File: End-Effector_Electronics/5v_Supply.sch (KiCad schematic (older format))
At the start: 0 parts

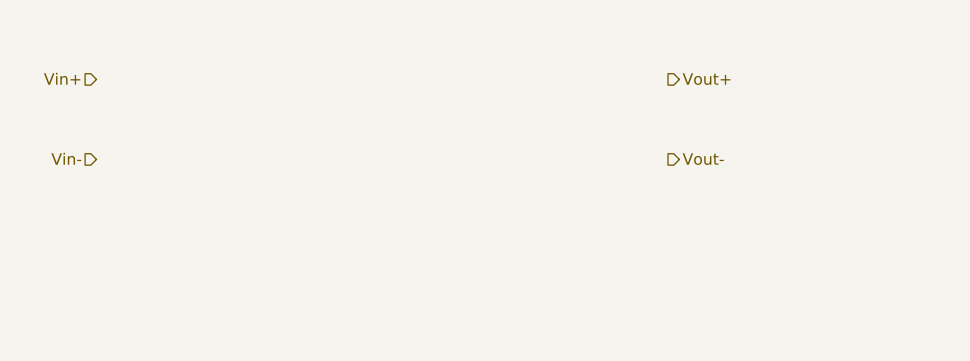
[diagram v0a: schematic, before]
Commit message: 5V supply added
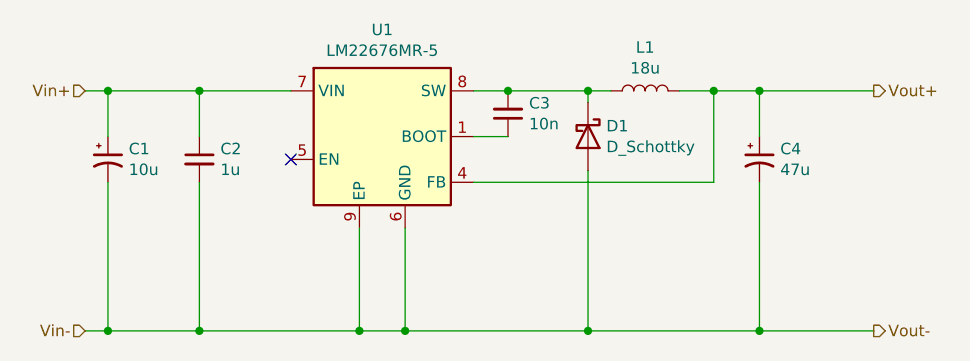
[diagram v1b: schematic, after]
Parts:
- added C1: 10u, symbol Device:CP1_Small
- added C2: 1u, symbol Device:C_Small
- added C3: 10n, symbol Device:C_Small
- added C4: 47u, symbol Device:CP1_Small
- added D1: D_Schottky, symbol Device:D_Schottky
- added L1: 18u, symbol Device:L
- added U1: LM22676MR-5, Package_SO:TI_SO-PowerPAD-8, symbol Regulator_Switching:LM22676MR-5
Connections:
- net Vin+: now also C1.1, C2.1, U1.7 (VIN)
- net Vin-: now also C1.2, C2.2, C4.2, D1.2 (A), U1.6 (GND), U1.9 (EP)
- net Vout+: now also C4.1, L1.2, U1.4 (FB)
- new net: C3.1, U1.1 (BOOT)
- new net: C3.2, D1.1 (K), L1.1, U1.8 (SW)
- no-connect marks 0 -> 1
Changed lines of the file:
@@
 Comment4 ""
 $EndDescr
-Text HLabel 4200 4100 0    50   Input ~ 0
+Text HLabel 4150 4850 0    50   Input ~ 0
 Vin-
-Text HLabel 4200 3750 0    50   Input ~ 0
+Text HLabel 4150 3800 0    50   Input ~ 0
 Vin+
-Text HLabel 6700 4100 2    50   Output ~ 0
+Text HLabel 7600 4850 2    50   Output ~ 0
 Vout-
-Text HLabel 6700 3750 2    50   Output ~ 0
+Text HLabel 7600 3800 2    50   Output ~ 0
 Vout+
+$Comp
+L Regulator_Switching:LM22676MR-5 U1
+U 1 1 617DB04C
+P 5450 4000
+F 0 "U1" H 5450 4467 50  0000 C CNN
+F 1 "LM22676MR-5" H 5450 4376 50  0000 C CNN
+F 2 "Package_SO:TI_SO-PowerPAD-8" H 5450 4450 50  0001 C CNN
+F 3 "http://www.ti.com/lit/ds/symlink/lm22676.pdf" H 5500 4000 50  0001 C CNN
+	1    5450 4000
+	1    0    0    -1
+$EndComp
+Wire Wire Line
+	4150 4850 4250 4850
+Wire Wire Line
+	5550 4850 5550 4400
+Wire Wire Line
+	5550 4850 6350 4850
+Connection ~ 5550 4850
+$Comp
+L Device:C_Small C3
+U 1 1 617DBA3C
+P 6000 3900
+F 0 "C3" H 5908 3854 50  0000 R CNN
+F 1 "10n" H 5908 3945 50  0000 R CNN
+F 2 "" H 6000 3900 50  0001 C CNN
+F 3 "~" H 6000 3900 50  0001 C CNN
+	1    6000 3900
+	-1   0    0    1
+$EndComp
+$Comp
+L Device:L L1
+U 1 1 617DBD4D
+P 6600 3800
+F 0 "L1" V 6790 3800 50  0000 C CNN
+F 1 "18u" V 6699 3800 50  0000 C CNN
+F 2 "" H 6600 3800 50  0001 C CNN
+F 3 "~" H 6600 3800 50  0001 C CNN
+	1    6600 3800
+	0    -1   -1   0
+$EndComp
+$Comp
+L Device:D_Schottky D1
+U 1 1 617DC8B2
+P 6350 4000
+F 0 "D1" V 6304 4080 50  0000 L CNN
+F 1 "D_Schottky" V 6395 4080 50  0000 L CNN
+F 2 "" H 6350 4000 50  0001 C CNN
+F 3 "~" H 6350 4000 50  0001 C CNN
+	1    6350 4000
+	0    1    1    0
+$EndComp
+$Comp
+L Device:C_Small C2
+U 1 1 617DCE06
+P 4650 4100
+F 0 "C2" H 4742 4146 50  0000 L CNN
+F 1 "1u" H 4742 4055 50  0000 L CNN
+F 2 "" H 4650 4100 50  0001 C CNN
+F 3 "~" H 4650 4100 50  0001 C CNN
+	1    4650 4100
+	1    0    0    -1
+$EndComp
+$Comp
+L Device:CP1_Small C1
+U 1 1 617DD0A0
+P 4250 4100
+F 0 "C1" H 4341 4146 50  0000 L CNN
+F 1 "10u" H 4341 4055 50  0000 L CNN
+F 2 "" H 4250 4100 50  0001 C CNN
+F 3 "~" H 4250 4100 50  0001 C CNN
+	1    4250 4100
+	1    0    0    -1
+$EndComp
+Wire Wire Line
+	4150 3800 4250 3800
+Wire Wire Line
+	4250 4000 4250 3800
+Connection ~ 4250 3800
+Wire Wire Line
+	4250 3800 4650 3800
+Wire Wire Line
+	4250 4200 4250 4850
+Connection ~ 4250 4850
+Wire Wire Line
+	4250 4850 4650 4850
+Wire Wire Line
+	4650 4200 4650 4850
+Connection ~ 4650 4850
+Wire Wire Line
+	4650 4850 5350 4850
+Wire Wire Line
+	4650 4000 4650 3800
+Connection ~ 4650 3800
+Wire Wire Line
+	4650 3800 5050 3800
+Wire Wire Line
+	5350 4400 5350 4850
+Connection ~ 5350 4850
+Wire Wire Line
+	5350 4850 5550 4850
+NoConn ~ 5050 4100
+Wire Wire Line
+	7600 3800 7100 3800
+Connection ~ 6350 3800
+Wire Wire Line
+	6350 3800 6000 3800
+Wire Wire Line
+	6350 3800 6350 3850
+Wire Wire Line
+	6350 4150 6350 4850
+Connection ~ 6350 4850
+Wire Wire Line
+	6450 3800 6350 3800
+Connection ~ 6000 3800
+Wire Wire Line
+	6000 3800 5850 3800
+Wire Wire Line
+	5850 4000 6000 4000
+Wire Wire Line
+	5850 4200 6900 4200
+Wire Wire Line
+	6900 4200 6900 3800
+Connection ~ 6900 3800
+Wire Wire Line
+	6900 3800 6750 3800
+Wire Wire Line
+	7100 4200 7100 4850
+Wire Wire Line
+	7100 4000 7100 3800
+$Comp
+L Device:CP1_Small C4
+U 1 1 617DBFA8
+P 7100 4100
+F 0 "C4" H 7191 4146 50  0000 L CNN
+F 1 "47u" H 7191 4055 50  0000 L CNN
+F 2 "" H 7100 4100 50  0001 C CNN
+F 3 "~" H 7100 4100 50  0001 C CNN
+	1    7100 4100
+	1    0    0    -1
+$EndComp
+Connection ~ 7100 3800
+Connection ~ 7100 4850
+Wire Wire Line
+	7100 4850 7600 4850
+Wire Wire Line
+	6350 4850 7100 4850
+Wire Wire Line
+	6900 3800 7100 3800
 $EndSCHEMATC
